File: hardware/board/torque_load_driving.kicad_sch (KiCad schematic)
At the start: 32 parts, among them J4 Conn_01x02_Female, Q2 Si7336ADP, U10 AD8615, U11 INA180A4, U12 AD8615, U17 LTC2641, U9 ADS7049

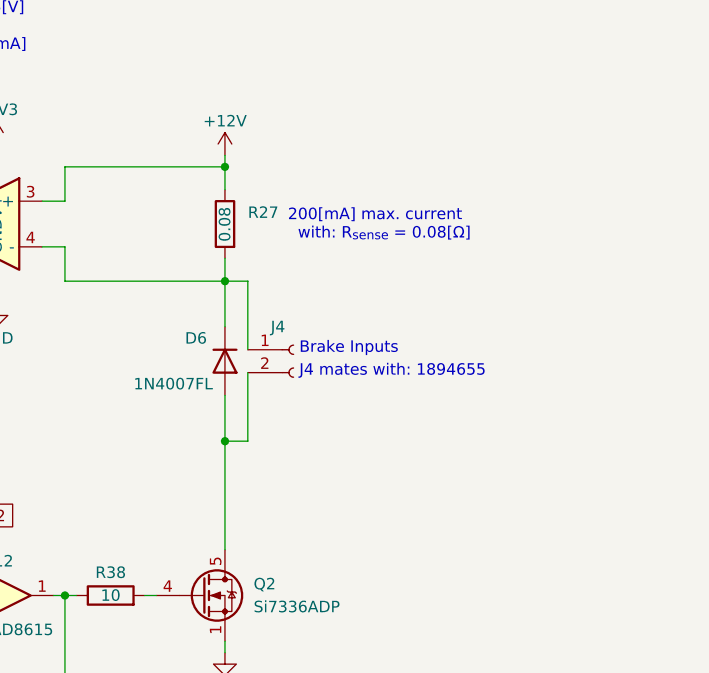
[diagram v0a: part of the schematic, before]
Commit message: add tvs diodes to inputs
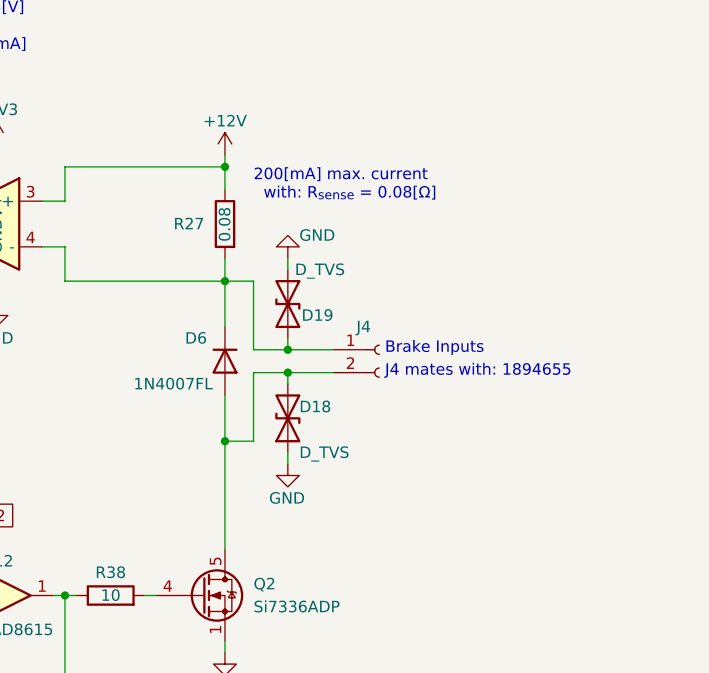
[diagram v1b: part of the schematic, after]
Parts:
- added D18, D19: D_TVS, Diode_SMD:D_SOD-882D, symbol Device:D_TVS
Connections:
- net GND: now also D18.1 (A1), D19.1 (A1)
- net at D6.1 (K), J4.1 (Pin_1), R27.2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: now also D19.2 (A2)
- net at D6.2 (A), J4.2 (Pin_2), Q2.5 (D): now also D18.2 (A2)
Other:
- moved on the sheet: J4
